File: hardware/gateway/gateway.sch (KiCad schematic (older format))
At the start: 32 parts, among them J1 FTDI, J2 Conn_Coaxial, J3 Raspberry_Pi_2_3, U1 RFM69HW, U2 MCP7940N-xSN, U3 AP130-xxY, Y1 32768 - 6pF

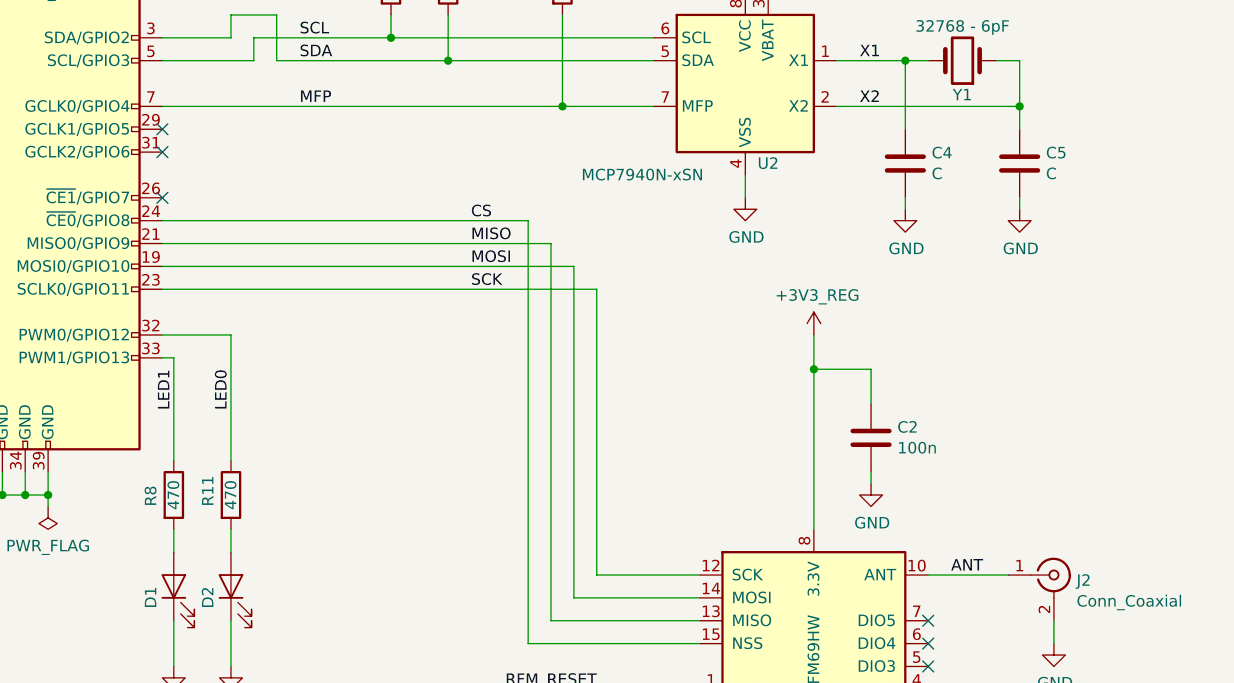
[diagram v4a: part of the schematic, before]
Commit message: Improved mounting holes and planes
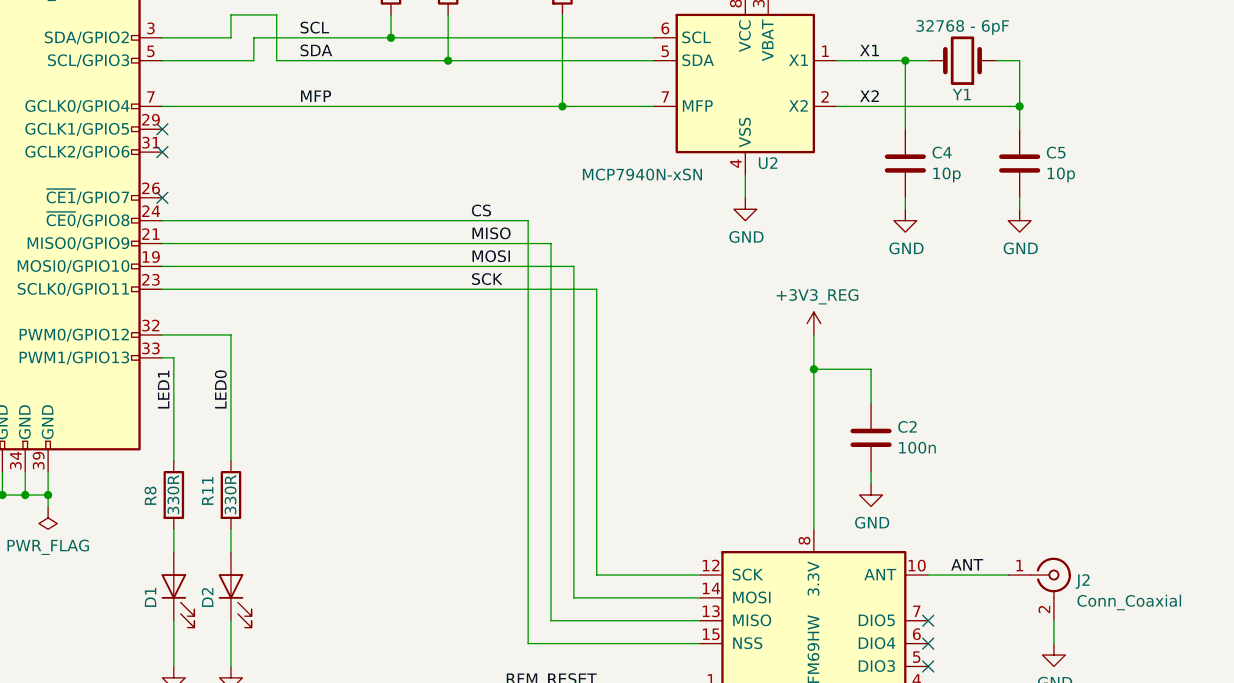
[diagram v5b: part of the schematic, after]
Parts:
- C2, C3, C7: TME Link (none) -> https://www.tme.eu/se/en/details/cl10b104ko8nnnc/0603-mlcc-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; TME Price (none) -> 0.13310
- C4, C5: value C -> 10p; TME Link (none) -> https://www.tme.eu/se/en/details/vj0603a100jxacw1bc/0603-ml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; TME Price (none) -> 0.13272
- D1: value LED -> KP-2012LSURCK; TME Link (none) -> https://www.tme.eu/se/en/details/kp-2012lsurck/smd-colour-l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; TME Price (none) -> 1.052
- D2: value LED -> KP-2012LSGC; TME Link (none) -> https://www.tme.eu/se/en/details/kp-2012lsgc/smd-colour-led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; TME Price (none) -> 0.24810
- H1, H2, H3, H4: footprint MountingHole:MountingHole_2.7mm_M2.5 -> humidity:MountingHole_2.7mm_M2.5
- R11, R8: value 470 -> 330R; TME Link (none) -> https://www.tme.eu/se/en/details/smd0603-330r-1%25/0603-smd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; TME Price (none) -> 0.11531
- R2, R3: TME Link (none) -> https://www.tme.eu/se/en/details/smd0603-0r/0603-smd-resist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; TME Price (none) -> 0.09735
- R5: TME Link (none) -> https://www.tme.eu/se/en/details/crcw060310k0fktabc/0603-sm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; TME Price (none) -> 0.12458
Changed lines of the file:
@@
 F 0 "H1" H 6250 6846 50  0000 L CNN
 F 1 "MountingHole" H 6250 6755 50  0000 L CNN
-F 2 "MountingHole:MountingHole_2.7mm_M2.5" H 6150 6800 50  0001 C CNN
+F 2 "humidity:MountingHole_2.7mm_M2.5" H 6150 6800 50  0001 C CNN
 F 3 "~" H 6150 6800 50  0001 C CNN
 	1    6150 6800
@@
 F 0 "H2" H 6250 7046 50  0000 L CNN
 F 1 "MountingHole" H 6250 6955 50  0000 L CNN
-F 2 "MountingHole:MountingHole_2.7mm_M2.5" H 6150 7000 50  0001 C CNN
+F 2 "humidity:MountingHole_2.7mm_M2.5" H 6150 7000 50  0001 C CNN
 F 3 "~" H 6150 7000 50  0001 C CNN
 	1    6150 7000
@@
 F 0 "H3" H 6250 7246 50  0000 L CNN
 F 1 "MountingHole" H 6250 7155 50  0000 L CNN
-F 2 "MountingHole:MountingHole_2.7mm_M2.5" H 6150 7200 50  0001 C CNN
+F 2 "humidity:MountingHole_2.7mm_M2.5" H 6150 7200 50  0001 C CNN
 F 3 "~" H 6150 7200 50  0001 C CNN
 	1    6150 7200
@@
 F 0 "H4" H 6250 7446 50  0000 L CNN
 F 1 "MountingHole" H 6250 7355 50  0000 L CNN
-F 2 "MountingHole:MountingHole_2.7mm_M2.5" H 6150 7400 50  0001 C CNN
+F 2 "humidity:MountingHole_2.7mm_M2.5" H 6150 7400 50  0001 C CNN
 F 3 "~" H 6150 7400 50  0001 C CNN
 	1    6150 7400
@@
 P 8950 2600
 F 0 "C5" H 9065 2646 50  0000 L CNN
-F 1 "C" H 9065 2555 50  0000 L CNN
+F 1 "10p" H 9065 2555 50  0000 L CNN
 F 2 "Capacitor_SMD:C_0603_1608Metric_Pad1.05x0.95mm_HandSolder" H 8988 2450 50  0001 C CNN
 F 3 "~" H 8950 2600 50  0001 C CNN
+F 4 "https://www.tme.eu/se/en/details/vj0603a100jxacw1bc/0603-mlcc-smd-capacitors/vishay/" H 0   0   50  0001 C CNN "TME Link"
+F 5 "0.13272" H 0   0   50  0001 C CNN "TME Price"
 	1    8950 2600
 	1    0    0    -1
@@
 P 8450 2600
 F 0 "C4" H 8565 2646 50  0000 L CNN
-F 1 "C" H 8565 2555 50  0000 L CNN
+F 1 "10p" H 8565 2555 50  0000 L CNN
 F 2 "Capacitor_SMD:C_0603_1608Metric_Pad1.05x0.95mm_HandSolder" H 8488 2450 50  0001 C CNN
 F 3 "~" H 8450 2600 50  0001 C CNN
+F 4 "https://www.tme.eu/se/en/details/vj0603a100jxacw1bc/0603-mlcc-smd-capacitors/vishay/" H 0   0   50  0001 C CNN "TME Link"
+F 5 "0.13272" H 0   0   50  0001 C CNN "TME Price"
 	1    8450 2600
 	1    0    0    -1
@@
 F 2 "Capacitor_SMD:C_0603_1608Metric_Pad1.05x0.95mm_HandSolder" H 7488 1250 50  0001 C CNN
 F 3 "~" H 7450 1400 50  0001 C CNN
+F 4 "https://www.tme.eu/se/en/details/cl10b104ko8nnnc/0603-mlcc-smd-capacitors/samsung/" H 0   0   50  0001 C CNN "TME Link"
+F 5 "0.13310" H 0   0   50  0001 C CNN "TME Price"
 	1    7450 1400
 	1    0    0    -1
@@
 F 2 "Resistor_SMD:R_0603_1608Metric_Pad1.05x0.95mm_HandSolder" V 2180 1050 50  0001 C CNN
 F 3 "~" H 2250 1050 50  0001 C CNN
+F 4 "https://www.tme.eu/se/en/details/smd0603-0r/0603-smd-resistors/royal-ohm/0603saj0000t5e/" H 0   0   50  0001 C CNN "TME Link"
+F 5 "0.09735" H 0   0   50  0001 C CNN "TME Price"
 	1    2250 1050
 	0    1    1    0
@@
 F 2 "Resistor_SMD:R_0603_1608Metric_Pad1.05x0.95mm_HandSolder" V 2180 1250 50  0001 C CNN
 F 3 "~" H 2250 1250 50  0001 C CNN
+F 4 "https://www.tme.eu/se/en/details/smd0603-0r/0603-smd-resistors/royal-ohm/0603saj0000t5e/" H 0   0   50  0001 C CNN "TME Link"
+F 5 "0.09735" H 0   0   50  0001 C CNN "TME Price"
 	1    2250 1250
 	0    1    1    0
@@
 F 2 "Capacitor_SMD:C_0603_1608Metric_Pad1.05x0.95mm_HandSolder" H 8338 3650 50  0001 C CNN
 F 3 "~" H 8300 3800 50  0001 C CNN
+F 4 "https://www.tme.eu/se/en/details/cl10b104ko8nnnc/0603-mlcc-smd-capacitors/samsung/" H 0   0   50  0001 C CNN "TME Link"
+F 5 "0.13310" H 0   0   50  0001 C CNN "TME Price"
 	1    8300 3800
 	1    0    0    -1
@@
 P 5500 4450
 F 0 "D2" H 5500 4550 50  0000 R CNN
-F 1 "LED" V 5447 4333 50  0001 R CNN
+F 1 "KP-2012LSGC" V 5447 4333 50  0001 R CNN
 F 2 "LED_SMD:LED_0805_2012Metric_Pad1.15x1.40mm_HandSolder" H 5500 4450 50  0001 C CNN
 F 3 "~" H 5500 4450 50  0001 C CNN
+F 4 "https://www.tme.eu/se/en/details/kp-2012lsgc/smd-colour-leds/kingbright-electronic/" H 0   0   50  0001 C CNN "TME Link"
+F 5 "0.24810" H 0   0   50  0001 C CNN "TME Price"
 	1    5500 4450
 	0    -1   -1   0
@@
 P 5500 4050
 F 0 "R11" V 5400 4000 50  0000 L CNN
-F 1 "470" V 5500 4050 50  0000 C CNN
+F 1 "330R" V 5500 4050 50  0000 C CNN
 F 2 "Resistor_SMD:R_0603_1608Metric_Pad1.05x0.95mm_HandSolder" V 5430 4050 50  0001 C CNN
 F 3 "~" H 5500 4050 50  0001 C CNN
+F 4 "https://www.tme.eu/se/en/details/smd0603-330r-1%25/0603-smd-resistors/royal-ohm/0603saf3300t5e/" H 0   0   50  0001 C CNN "TME Link"
+F 5 "0.11531" H 0   0   50  0001 C CNN "TME Price"
 	1    5500 4050
 	1    0    0    -1
@@
 P 5250 4450
 F 0 "D1" H 5250 4550 50  0000 R CNN
-F 1 "LED" V 5197 4333 50  0001 R CNN
+F 1 "KP-2012LSURCK" V 5197 4333 50  0001 R CNN
 F 2 "LED_SMD:LED_0805_2012Metric_Pad1.15x1.40mm_HandSolder" H 5250 4450 50  0001 C CNN
 F 3 "~" H 5250 4450 50  0001 C CNN
+F 4 "https://www.tme.eu/se/en/details/kp-2012lsurck/smd-colour-leds/kingbright-electronic/" H 0   0   50  0001 C CNN "TME Link"
+F 5 "1.052" H 0   0   50  0001 C CNN "TME Price"
 	1    5250 4450
 	0    -1   -1   0
@@
 P 5250 4050
 F 0 "R8" V 5150 4000 50  0000 L CNN
-F 1 "470" V 5250 4050 50  0000 C CNN
+F 1 "330R" V 5250 4050 50  0000 C CNN
 F 2 "Resistor_SMD:R_0603_1608Metric_Pad1.05x0.95mm_HandSolder" V 5180 4050 50  0001 C CNN
 F 3 "~" H 5250 4050 50  0001 C CNN
+F 4 "https://www.tme.eu/se/en/details/smd0603-330r-1%25/0603-smd-resistors/royal-ohm/0603saf3300t5e/" H 0   0   50  0001 C CNN "TME Link"
+F 5 "0.11531" H 0   0   50  0001 C CNN "TME Price"
 	1    5250 4050
 	1    0    0    -1
@@
 F 2 "Capacitor_SMD:C_0603_1608Metric_Pad1.05x0.95mm_HandSolder" H 8188 1250 50  0001 C CNN
 F 3 "~" H 8150 1400 50  0001 C CNN
+F 4 "https://www.tme.eu/se/en/details/cl10b104ko8nnnc/0603-mlcc-smd-capacitors/samsung/" H 0   0   50  0001 C CNN "TME Link"
+F 5 "0.13310" H 0   0   50  0001 C CNN "TME Price"
 	1    8150 1400
 	1    0    0    -1
@@
 F 2 "Resistor_SMD:R_0603_1608Metric_Pad1.05x0.95mm_HandSolder" V 6880 1800 50  0001 C CNN
 F 3 "~" H 6950 1800 50  0001 C CNN
+F 4 "https://www.tme.eu/se/en/details/crcw060310k0fktabc/0603-smd-resistors/vishay/" H 0   0   50  0001 C CNN "TME Link"
+F 5 "0.12458" H 0   0   50  0001 C CNN "TME Price"
 	1    6950 1800
 	1    0    0    -1

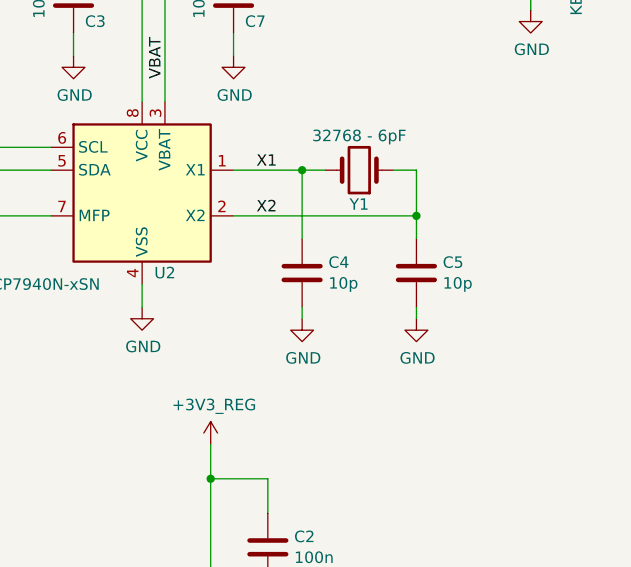
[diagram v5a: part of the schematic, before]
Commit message: Improved optional resistors
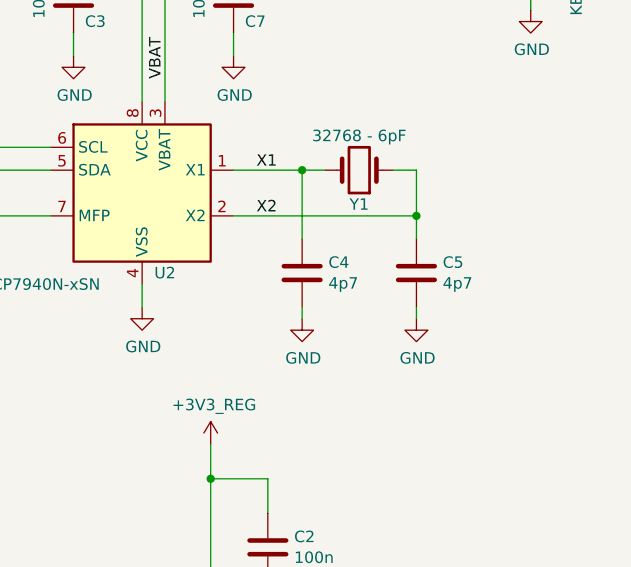
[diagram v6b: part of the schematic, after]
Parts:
- C4, C5: value 10p -> 4p7; TME Link https://www.tme.eu/se/en/details/vj0603a100jxacw1bc/0603-ml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 -> https://www.tme.eu/se/en/details/c0603c479c1gactu/0603-mlcc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; TME Price 0.13272 -> 0.77794
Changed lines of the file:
@@
 	7750 2650 7750 2750
-$Comp
-L Device:C C5
-U 1 1 5CF7C57B
-P 8950 2600
-F 0 "C5" H 9065 2646 50  0000 L CNN
-F 1 "10p" H 9065 2555 50  0000 L CNN
-F 2 "Capacitor_SMD:C_0603_1608Metric_Pad1.05x0.95mm_HandSolder" H 8988 2450 50  0001 C CNN
-F 3 "~" H 8950 2600 50  0001 C CNN
-F 4 "https://www.tme.eu/se/en/details/vj0603a100jxacw1bc/0603-mlcc-smd-capacitors/vishay/" H 0   0   50  0001 C CNN "TME Link"
-F 5 "0.13272" H 0   0   50  0001 C CNN "TME Price"
-	1    8950 2600
-	1    0    0    -1
-$EndComp
 $Comp
 L Device:C C4
@@
 P 8450 2600
 F 0 "C4" H 8565 2646 50  0000 L CNN
-F 1 "10p" H 8565 2555 50  0000 L CNN
+F 1 "4p7" H 8565 2555 50  0000 L CNN
 F 2 "Capacitor_SMD:C_0603_1608Metric_Pad1.05x0.95mm_HandSolder" H 8488 2450 50  0001 C CNN
 F 3 "~" H 8450 2600 50  0001 C CNN
-F 4 "https://www.tme.eu/se/en/details/vj0603a100jxacw1bc/0603-mlcc-smd-capacitors/vishay/" H 0   0   50  0001 C CNN "TME Link"
-F 5 "0.13272" H 0   0   50  0001 C CNN "TME Price"
+F 4 "https://www.tme.eu/se/en/details/c0603c479c1gactu/0603-mlcc-smd-capacitors/kemet/" H 0   0   50  0001 C CNN "TME Link"
+F 5 "0.77794" H 0   0   50  0001 C CNN "TME Price"
 	1    8450 2600
 	1    0    0    -1
@@
 Text Label 6550 3150 0    50   ~ 0
 SCK
+$Comp
+L Device:C C5
+U 1 1 5D0FD74D
+P 8950 2600
+F 0 "C5" H 9065 2646 50  0000 L CNN
+F 1 "4p7" H 9065 2555 50  0000 L CNN
+F 2 "Capacitor_SMD:C_0603_1608Metric_Pad1.05x0.95mm_HandSolder" H 8988 2450 50  0001 C CNN
+F 3 "~" H 8950 2600 50  0001 C CNN
+F 4 "https://www.tme.eu/se/en/details/c0603c479c1gactu/0603-mlcc-smd-capacitors/kemet/" H 500 0   50  0001 C CNN "TME Link"
+F 5 "0.77794" H 500 0   50  0001 C CNN "TME Price"
+	1    8950 2600
+	1    0    0    -1
+$EndComp
 $EndSCHEMATC

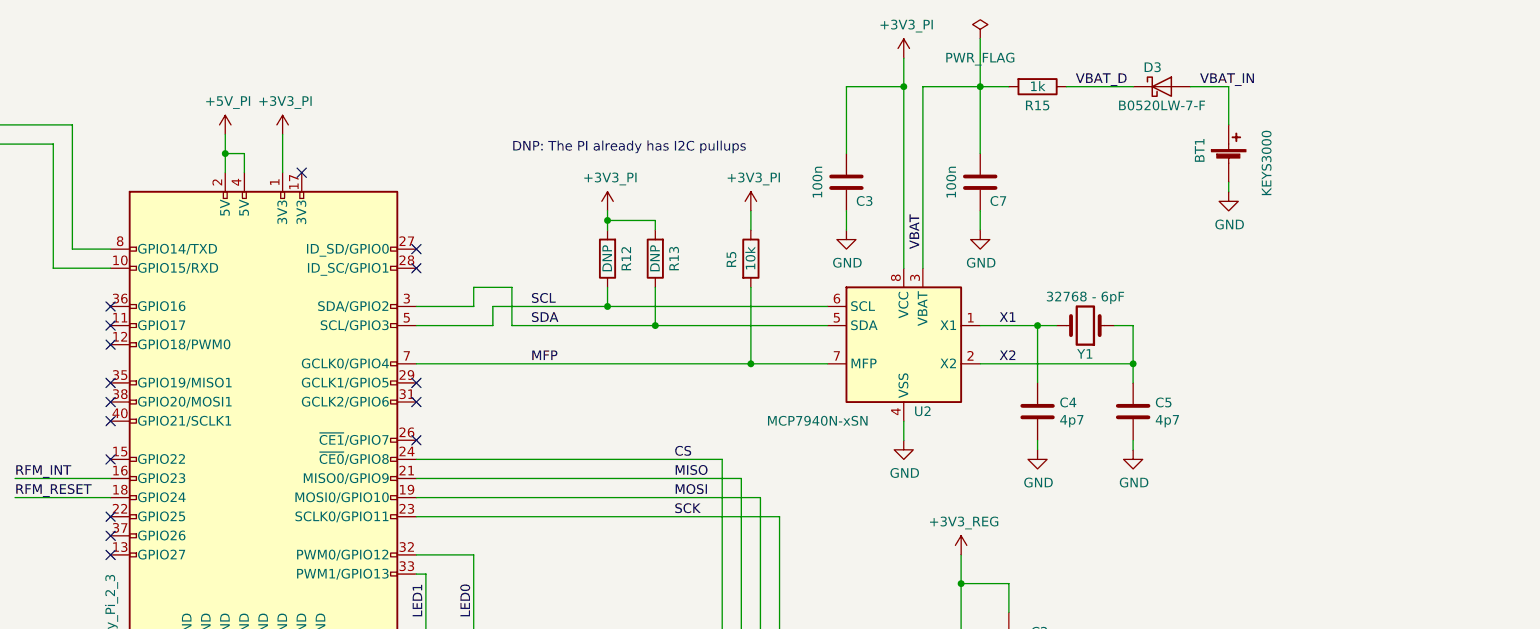
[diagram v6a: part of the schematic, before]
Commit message: DS1307 and PTH crystal
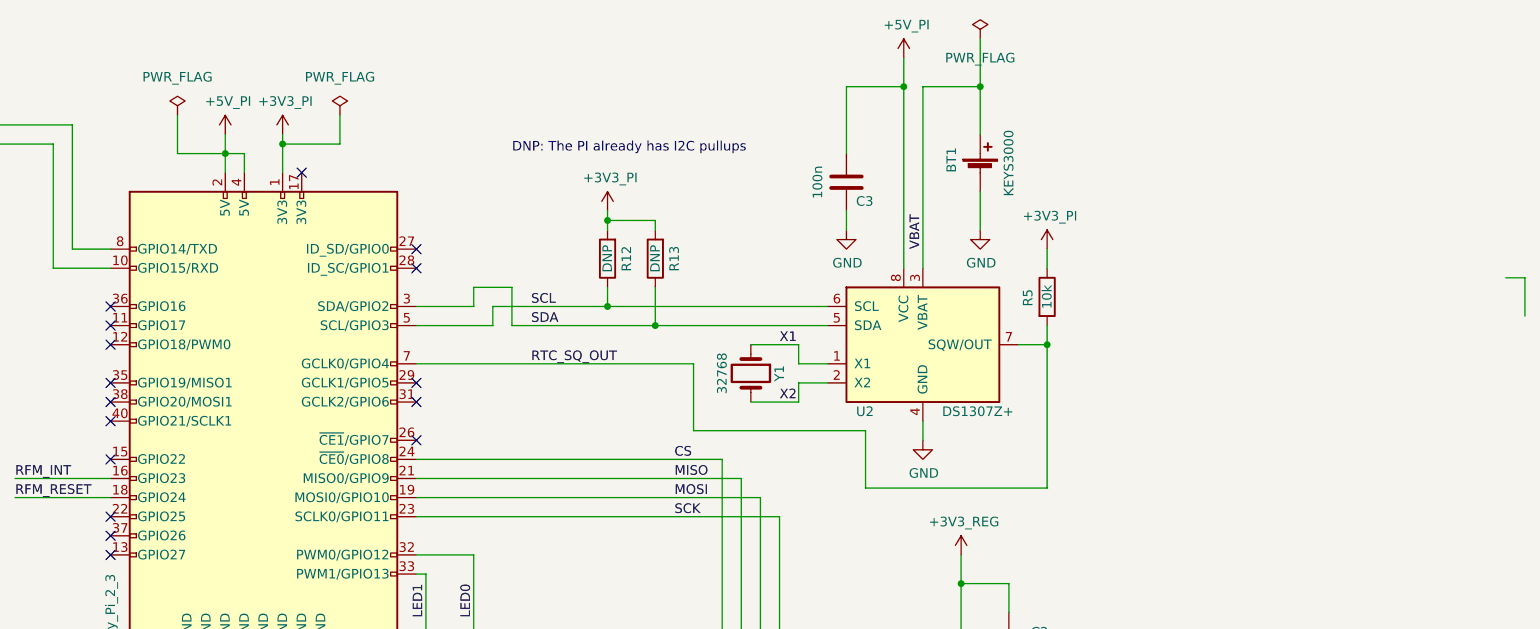
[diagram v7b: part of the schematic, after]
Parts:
- removed C4, C5: 4p7, Capacitor_SMD:C_0603_1608Metric_Pad1.05x0.95mm_HandSolder, symbol Device:C
- removed C7: 100n, Capacitor_SMD:C_0603_1608Metric_Pad1.05x0.95mm_HandSolder, symbol Device:C
- removed D3: B0520LW-7-F, Diode_SMD:D_SOD-123, symbol Device:D_Schottky
- removed R15: 1k, Resistor_SMD:R_0603_1608Metric_Pad1.05x0.95mm_HandSolder, symbol Device:R
- removed U2: MCP7940N-xSN, Package_SO:SOIC-8_3.9x4.9mm_P1.27mm, symbol Timer:MCP7940N-xSN
- added U2: DS1307Z+, Package_SO:SOIC-8_3.9x4.9mm_P1.27mm, symbol Timer_RTC:DS1307Z+
- Y1: value 32768 - 6pF -> 32768; footprint humidity:Crystal LFXTAL016178 -> Crystal:Crystal_C26-LF_D2.1mm_L6.5mm_Horizontal; TME Link https://www.tme.eu/se/en/details/32.768k-85smxr/smd-quartz-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 -> https://www.tme.eu/se/en/details/26-hx5f-32.768k/tht-quartz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; TME Price 6.09368 -> 1.52097
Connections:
- net VBAT_IN is gone; now on net VBAT: BT1.1 (+)
- net +3V3_PI: no longer C3.1
- net +5V_PI: now also C3.1, U2.8 (VCC)
- net GND: now also U2.4 (GND)
- net SCL: now also U2.6 (SCL)
- net SDA: now also U2.5 (SDA)
- net VBAT: now also U2.3 (VBAT)
- net X1: now also Y1.1, U2.1 (X1); no longer Y1.2
- net X2: now also Y1.2, U2.2 (X2); no longer Y1.1
- net MFP renamed RTC_SQ_OUT
- net RTC_SQ_OUT: now also U2.7 (SQW/OUT)
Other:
- moved on the sheet: BT1, R5, Y1
